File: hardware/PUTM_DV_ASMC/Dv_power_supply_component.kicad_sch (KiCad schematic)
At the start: 24 parts, among them IC2 BTS722204ESAXUMA1

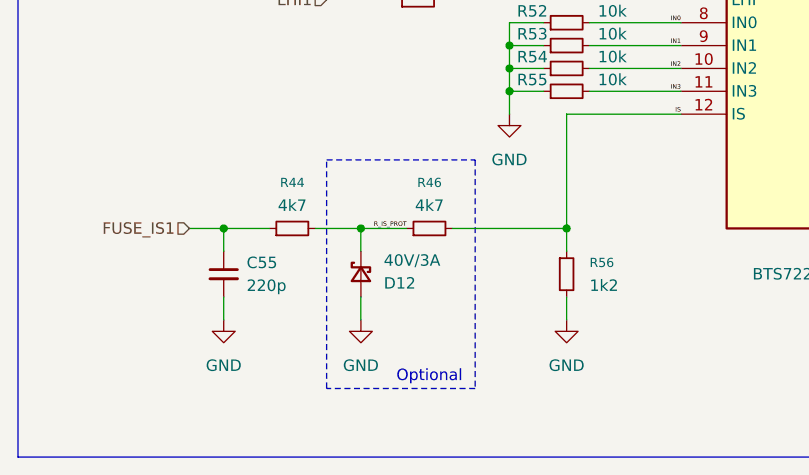
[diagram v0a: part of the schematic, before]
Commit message: tylko dwa bledy z can - schemat na wykonczeniu
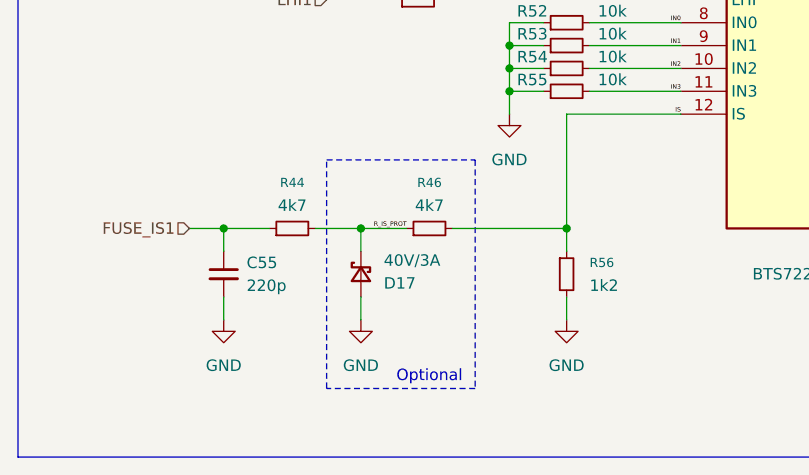
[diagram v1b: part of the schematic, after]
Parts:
- renumbered D12 to D17
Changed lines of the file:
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@@
 		(in_pos_files yes)
 		(dnp no)
-		(property "Reference" "D12"
+		(property "Reference" "D17"
 			(at 110.49 126.7461 90)
 			(show_name no)
@@
 			(project "PUTM_DV_ASMC"
 				(path "/b652b05a-4e3d-4ad1-b032-18886abe7d45/df6a7f0c-3e94-451b-97ae-08b4f03339fc/79a9e11a-2c17-464a-b0de-26bb2a26fbe1"
-					(reference "D12")
+					(reference "D17")
 					(unit 1)
 				)
@@
 		(dnp no)
 		(fields_autoplaced yes)
-		(property "Reference" "#PWR067"
+		(property "Reference" "#PWR074"
 			(at 92.71 137.16 0)
 			(hide yes)
@@
 			(project "PUTM_DV_ASMC"
 				(path "/b652b05a-4e3d-4ad1-b032-18886abe7d45/df6a7f0c-3e94-451b-97ae-08b4f03339fc/79a9e11a-2c17-464a-b0de-26bb2a26fbe1"
-					(reference "#PWR067")
+					(reference "#PWR074")
 					(unit 1)
 				)
@@
 		(dnp no)
 		(fields_autoplaced yes)
-		(property "Reference" "#PWR068"
+		(property "Reference" "#PWR075"
 			(at 104.14 83.82 0)
 			(hide yes)
@@
 			(project "PUTM_DV_ASMC"
 				(path "/b652b05a-4e3d-4ad1-b032-18886abe7d45/df6a7f0c-3e94-451b-97ae-08b4f03339fc/79a9e11a-2c17-464a-b0de-26bb2a26fbe1"
-					(reference "#PWR068")
+					(reference "#PWR075")
 					(unit 1)
 				)
@@
 		(dnp no)
 		(fields_autoplaced yes)
-		(property "Reference" "#PWR073"
+		(property "Reference" "#PWR080"
 			(at 185.42 128.27 0)
 			(hide yes)
@@
 			(project "PUTM_DV_ASMC"
 				(path "/b652b05a-4e3d-4ad1-b032-18886abe7d45/df6a7f0c-3e94-451b-97ae-08b4f03339fc/79a9e11a-2c17-464a-b0de-26bb2a26fbe1"
-					(reference "#PWR073")
+					(reference "#PWR080")
 					(unit 1)
 				)
@@
 		(dnp no)
 		(fields_autoplaced yes)
-		(property "Reference" "#PWR069"
+		(property "Reference" "#PWR076"
 			(at 107.95 137.16 0)
 			(hide yes)
@@
 			(project "PUTM_DV_ASMC"
 				(path "/b652b05a-4e3d-4ad1-b032-18886abe7d45/df6a7f0c-3e94-451b-97ae-08b4f03339fc/79a9e11a-2c17-464a-b0de-26bb2a26fbe1"
-					(reference "#PWR069")
+					(reference "#PWR076")
 					(unit 1)
 				)
@@
 		(dnp no)
 		(fields_autoplaced yes)
-		(property "Reference" "#PWR070"
+		(property "Reference" "#PWR077"
 			(at 124.46 114.3 0)
 			(hide yes)
@@
 			(project "PUTM_DV_ASMC"
 				(path "/b652b05a-4e3d-4ad1-b032-18886abe7d45/df6a7f0c-3e94-451b-97ae-08b4f03339fc/79a9e11a-2c17-464a-b0de-26bb2a26fbe1"
-					(reference "#PWR070")
+					(reference "#PWR077")
 					(unit 1)
 				)
@@
 		(dnp no)
 		(fields_autoplaced yes)
-		(property "Reference" "#PWR072"
+		(property "Reference" "#PWR079"
 			(at 130.81 137.16 0)
 			(hide yes)
@@
 			(project "PUTM_DV_ASMC"
 				(path "/b652b05a-4e3d-4ad1-b032-18886abe7d45/df6a7f0c-3e94-451b-97ae-08b4f03339fc/79a9e11a-2c17-464a-b0de-26bb2a26fbe1"
-					(reference "#PWR072")
+					(reference "#PWR079")
 					(unit 1)
 				)
@@
 		(dnp no)
 		(fields_autoplaced yes)
-		(property "Reference" "#PWR071"
+		(property "Reference" "#PWR078"
 			(at 128.27 78.74 0)
 			(hide yes)
@@
 			(project "PUTM_DV_ASMC"
 				(path "/b652b05a-4e3d-4ad1-b032-18886abe7d45/df6a7f0c-3e94-451b-97ae-08b4f03339fc/79a9e11a-2c17-464a-b0de-26bb2a26fbe1"
-					(reference "#PWR071")
+					(reference "#PWR078")
 					(unit 1)
 				)

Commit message: poprawki footprint
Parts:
- IC2: footprint PDM:SOP65P600X115-25N -> BTS722204ESAXUMA1:SOP65P600X115-25N
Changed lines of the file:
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@@
 			)
 		)
-		(property "Footprint" "PDM:SOP65P600X115-25N"
+		(property "Footprint" "BTS722204ESAXUMA1:SOP65P600X115-25N"
 			(at 175.26 174.93 0)
 			(hide yes)
